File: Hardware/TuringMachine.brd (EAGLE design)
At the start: 107 x 49.5 mm, 83 parts, among them IC1 TL072P, IC2 4015, IC3 4015, IC5 4016, IC6 TL072P, IC7 TL072P, T1 2N3904, T2 2N3904, T3 2N3904

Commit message: Update R32 in noise and R6 in CV input
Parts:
- R32: value 10k -> 1k
- R6: value 150k -> 47k
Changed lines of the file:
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@@
 <grid distance="50" unitdist="mil" unit="mil" style="dots" multiple="1" display="no" altdistance="25" altunitdist="mil" altunit="mil"/>
 <layers>
-<layer number="1" name="Top" color="4" fill="1" visible="yes" active="yes"/>
+<layer number="1" name="Top" color="4" fill="1" visible="no" active="yes"/>
 <layer number="2" name="Route2" color="1" fill="3" visible="no" active="yes"/>
 <layer number="3" name="Route3" color="4" fill="3" visible="no" active="no"/>
 <layer number="14" name="Route14" color="1" fill="6" visible="no" active="no"/>
 <layer number="15" name="Route15" color="4" fill="6" visible="no" active="yes"/>
-<layer number="16" name="Bottom" color="1" fill="1" visible="yes" active="yes"/>
+<layer number="16" name="Bottom" color="1" fill="1" visible="no" active="yes"/>
 <layer number="17" name="Pads" color="10" fill="1" visible="yes" active="yes"/>
 <layer number="18" name="Vias" color="2" fill="1" visible="yes" active="yes"/>
@@
 <element name="R30" library="TomW" package="0207/7" value="10k" x="35.56" y="11.43"/>
 <element name="R31" library="TomW" package="0207/7" value="470k" x="45.72" y="12.7"/>
-<element name="R32" library="TomW" package="0207/7" value="10k" x="55.88" y="19.05"/>
+<element name="R32" library="TomW" package="0207/7" value="1k" x="55.88" y="19.05"/>
 <element name="NOISE-OUT" library="MusicThingModular" package="THONKICONN" value="THONKICONN" x="6.35" y="18.415" locked="yes" rot="R90"/>
 <element name="C2" library="TomW" package="C050-024X044" value="1n" x="17.145" y="38.1"/>
@@
 <element name="CV_IN" library="MusicThingModular" package="THONKICONN" value="THONKICONN" x="6.35" y="31.115" locked="yes" rot="R90"/>
 <element name="R5" library="TomW" package="0207/7" value="51k" x="5.715" y="24.765"/>
-<element name="R6" library="TomW" package="0207/7" value="150k" x="69.85" y="12.7"/>
+<element name="R6" library="TomW" package="0207/7" value="47k" x="69.85" y="12.7"/>
 <element name="CV_OUT" library="MusicThingModular" package="THONKICONN" value="THONKICONN" x="6.35" y="5.715" locked="yes" rot="R90"/>
 <element name="C13" library="TomW" package="C050-024X044" value="100n" x="66.04" y="33.02" rot="R90"/>

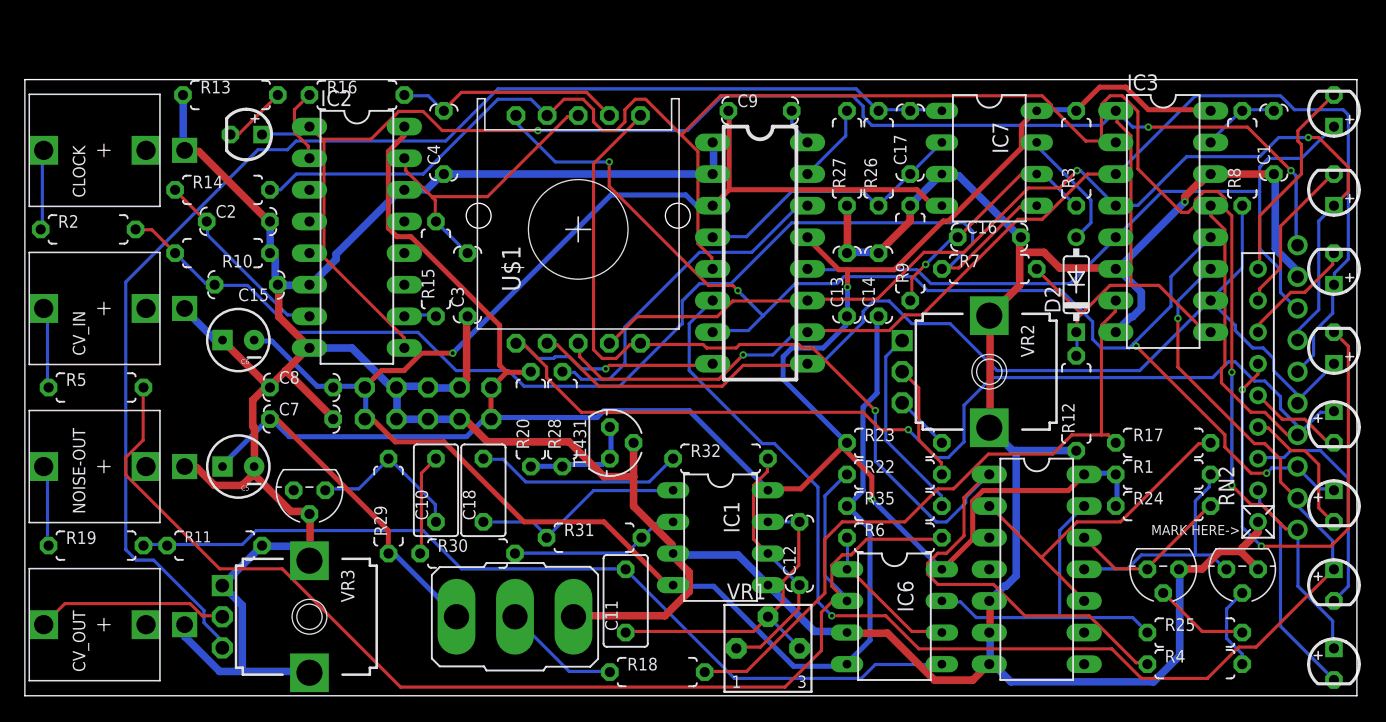
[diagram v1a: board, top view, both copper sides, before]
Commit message: Move R16 & C4 to start of loop
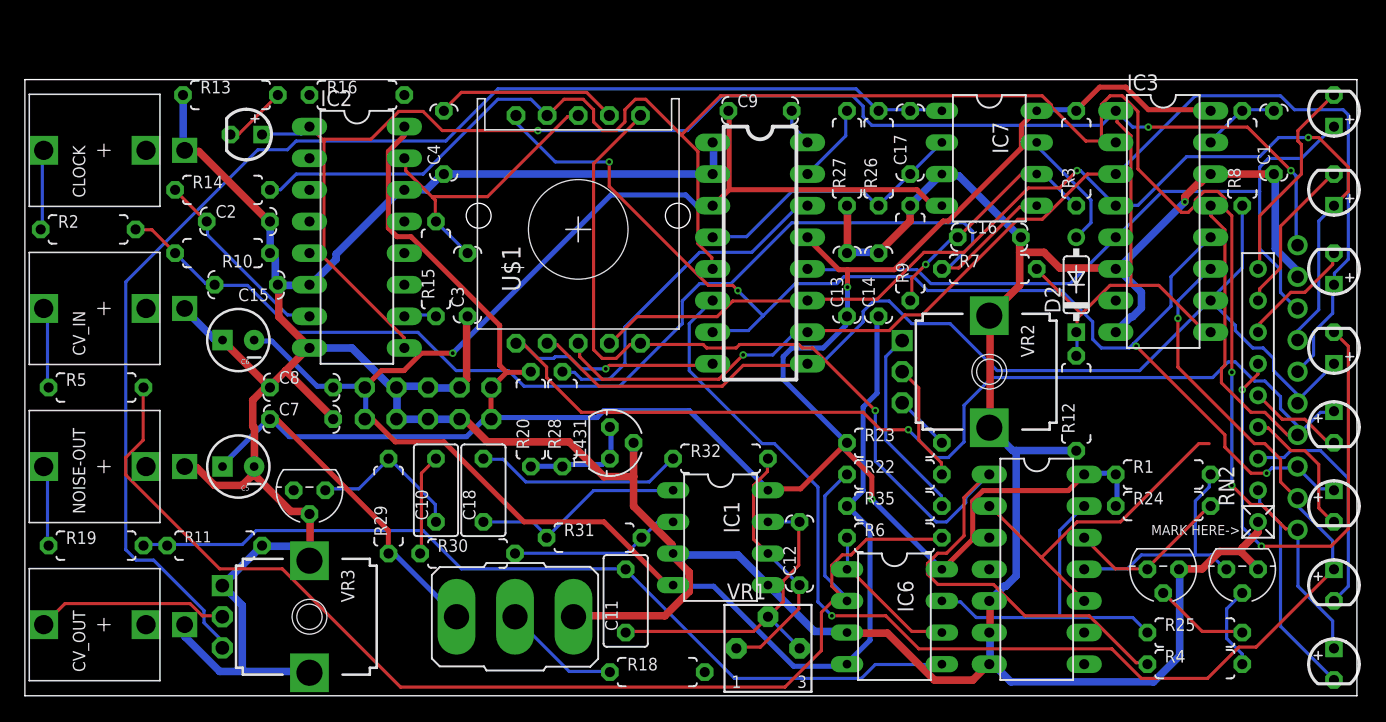
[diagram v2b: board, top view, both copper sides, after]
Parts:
- removed R17: 1k, TomW:0207/7
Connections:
- removed net N$19: IC3.7, R17.1, R18.2
- removed net N$29: IC2.2, R16.1
- net START_OF_LOOP: now also C4.2, IC3.7, R16.1, R16.2, R18.2; no longer R17.2
- net STEP_16: now also IC2.2; no longer C4.2, R16.2
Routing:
- net N$19: track 55.0 -> 0.00 mm
- net N$29: track 6.08 -> 0.00 mm
- net STEP_16: track 18.4 -> 14.6 mm
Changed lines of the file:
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@@
 <grid distance="50" unitdist="mil" unit="mil" style="dots" multiple="1" display="no" altdistance="25" altunitdist="mil" altunit="mil"/>
 <layers>
-<layer number="1" name="Top" color="4" fill="1" visible="no" active="yes"/>
+<layer number="1" name="Top" color="4" fill="1" visible="yes" active="yes"/>
 <layer number="2" name="Route2" color="1" fill="3" visible="no" active="yes"/>
 <layer number="3" name="Route3" color="4" fill="3" visible="no" active="no"/>
 <layer number="14" name="Route14" color="1" fill="6" visible="no" active="no"/>
 <layer number="15" name="Route15" color="4" fill="6" visible="no" active="yes"/>
-<layer number="16" name="Bottom" color="1" fill="1" visible="no" active="yes"/>
+<layer number="16" name="Bottom" color="1" fill="1" visible="yes" active="yes"/>
 <layer number="17" name="Pads" color="10" fill="1" visible="yes" active="yes"/>
 <layer number="18" name="Vias" color="2" fill="1" visible="yes" active="yes"/>
-<layer number="19" name="Unrouted" color="6" fill="1" visible="yes" active="yes"/>
+<layer number="19" name="Unrouted" color="6" fill="1" visible="no" active="yes"/>
 <layer number="20" name="Dimension" color="15" fill="1" visible="yes" active="yes"/>
 <layer number="21" name="tPlace" color="7" fill="1" visible="yes" active="yes"/>
-<layer number="22" name="bPlace" color="7" fill="1" visible="yes" active="yes"/>
-<layer number="23" name="tOrigins" color="15" fill="1" visible="yes" active="yes"/>
-<layer number="24" name="bOrigins" color="15" fill="1" visible="yes" active="yes"/>
+<layer number="22" name="bPlace" color="7" fill="1" visible="no" active="yes"/>
+<layer number="23" name="tOrigins" color="15" fill="1" visible="no" active="yes"/>
+<layer number="24" name="bOrigins" color="15" fill="1" visible="no" active="yes"/>
 <layer number="25" name="tNames" color="7" fill="1" visible="yes" active="yes"/>
 <layer number="26" name="bNames" color="7" fill="1" visible="no" active="yes"/>
-<layer number="27" name="tValues" color="7" fill="1" visible="no" active="yes"/>
+<layer number="27" name="tValues" color="7" fill="1" visible="yes" active="yes"/>
 <layer number="28" name="bValues" color="7" fill="1" visible="no" active="yes"/>
 <layer number="29" name="tStop" color="7" fill="3" visible="no" active="yes"/>
@@
 <layer number="49" name="Reference" color="7" fill="1" visible="no" active="yes"/>
 <layer number="50" name="dxf" color="7" fill="1" visible="no" active="no"/>
-<layer number="51" name="tDocu" color="7" fill="1" visible="yes" active="yes"/>
+<layer number="51" name="tDocu" color="7" fill="1" visible="no" active="yes"/>
 <layer number="52" name="bDocu" color="7" fill="1" visible="no" active="yes"/>
 <layer number="53" name="tGND_GNDA" color="7" fill="9" visible="no" active="no"/>
@@
 <element name="R9" library="TomW" package="0207/7" value="15k" x="71.12" y="35.56" rot="R90"/>
 <element name="WRITE" library="TomW" package="M9040P" value="T-80-T-SPDT-ON-OFF-ON" x="39.37" y="6.35" smashed="yes" rot="R90"/>
-<element name="R17" library="TomW" package="0207/7" value="1k" x="91.44" y="20.32"/>
 <element name="R18" library="TomW" package="0207/7" value="1k" x="50.8" y="1.905"/>
 <element name="EXPANSION" library="TomW" package="MA10-1" value="" x="102.235" y="24.765" locked="yes" rot="MR90">
@@
 </signal>
 <signal name="STEP_16">
-<contactref element="R16" pad="2"/>
-<contactref element="C4" pad="2"/>
 <contactref element="U$1" pad="H"/>
-<wire x1="32.4104" y1="48.1965" x2="30.5943" y2="48.1965" width="0.254" layer="16"/>
-<wire x1="33.528" y1="47.0789" x2="32.4104" y2="48.1965" width="0.254" layer="16"/>
-<wire x1="30.5943" y1="48.1965" x2="30.48" y2="48.26" width="0.254" layer="16"/>
-<wire x1="33.528" y1="47.0789" x2="33.655" y2="46.99" width="0.254" layer="16"/>
 <wire x1="45.1231" y1="48.4759" x2="46.9392" y2="46.6598" width="0.254" layer="1"/>
 <wire x1="35.0647" y1="48.4759" x2="45.1231" y2="48.4759" width="0.254" layer="1"/>
 <wire x1="33.6677" y1="47.0789" x2="35.0647" y2="48.4759" width="0.254" layer="1"/>
 <wire x1="46.9392" y1="46.6598" x2="46.95" y2="46.615" width="0.254" layer="1"/>
-<wire x1="33.6677" y1="47.0789" x2="33.655" y2="46.99" width="0.254" layer="1"/>
-</signal>
-<signal name="N$19">
-<contactref element="IC3" pad="7"/>
-<contactref element="R17" pad="1"/>
-<contactref element="R18" pad="2"/>
-<wire x1="57.9755" y1="1.9558" x2="54.6227" y2="1.9558" width="0.254" layer="1"/>
-<wire x1="64.262" y1="8.2423" x2="57.9755" y2="1.9558" width="0.254" layer="1"/>
-<wire x1="64.262" y1="12.573" x2="64.262" y2="8.2423" width="0.254" layer="1"/>
-<wire x1="65.659" y1="13.97" x2="64.262" y2="12.573" width="0.254" layer="1"/>
-<wire x1="70.6882" y1="13.97" x2="65.659" y2="13.97" width="0.254" layer="1"/>
-<wire x1="73.3425" y1="16.6243" x2="70.6882" y2="13.97" width="0.254" layer="1"/>
-<wire x1="74.5998" y1="16.6243" x2="73.3425" y2="16.6243" width="0.254" layer="1"/>
-<wire x1="77.3938" y1="19.4183" x2="74.5998" y2="16.6243" width="0.254" layer="1"/>
-<wire x1="82.5627" y1="19.4183" x2="77.3938" y2="19.4183" width="0.254" layer="1"/>
-<wire x1="84.0994" y1="20.955" x2="82.5627" y2="19.4183" width="0.254" layer="1"/>
-<wire x1="87.0331" y1="20.955" x2="86.4743" y2="20.955" width="0.254" layer="1"/>
-<wire x1="86.4743" y1="20.955" x2="84.0994" y2="20.955" width="0.254" layer="1"/>
-<wire x1="87.5919" y1="20.3962" x2="87.0331" y2="20.955" width="0.254" layer="1"/>
-<wire x1="54.6227" y1="1.9558" x2="54.61" y2="1.905" width="0.254" layer="1"/>
-<wire x1="87.5919" y1="20.3962" x2="87.63" y2="20.32" width="0.254" layer="1"/>
-<wire x1="87.5919" y1="30.8737" x2="87.5919" y2="31.7119" width="0.254" layer="1"/>
-<wire x1="86.4743" y1="29.7561" x2="87.5919" y2="30.8737" width="0.254" layer="1"/>
-<wire x1="86.4743" y1="20.955" x2="86.4743" y2="29.7561" width="0.254" layer="1"/>
-<wire x1="87.5919" y1="31.7119" x2="87.63" y2="31.75" width="0.254" layer="1"/>
+<contactref element="IC2" pad="2"/>
+<wire x1="22.86" y1="43.18" x2="33.6677" y2="47.0789" width="0" layer="19" extent="1-1"/>
 </signal>
 <signal name="B5">
@@
 </signal>
 <signal name="START_OF_LOOP">
-<contactref element="R17" pad="2"/>
 <contactref element="IC5" pad="10"/>
 <contactref element="IC5" pad="2"/>
@@
 <wire x1="84.5185" y1="13.97" x2="88.011" y2="13.97" width="0.254" layer="1"/>
 <wire x1="81.65465" y1="11.10615" x2="84.5185" y2="13.97" width="0.254" layer="1"/>
-<wire x1="95.1357" y1="20.2565" x2="95.25" y2="20.32" width="0.254" layer="1"/>
+<contactref element="R18" pad="2"/>
+<contactref element="IC3" pad="7"/>
+<contactref element="R16" pad="2"/>
+<contactref element="R16" pad="1"/>
+<contactref element="C4" pad="2"/>
+<wire x1="94.2975" y1="20.2565" x2="87.63" y2="31.75" width="0" layer="19" extent="1-1"/>
+<wire x1="54.61" y1="1.905" x2="77.47" y2="15.24" width="0" layer="19" extent="1-1"/>
+<wire x1="33.655" y1="46.99" x2="54.61" y2="1.905" width="0" layer="19" extent="1-1"/>
+<wire x1="30.48" y1="48.26" x2="33.655" y2="46.99" width="0" layer="19" extent="1-1"/>
+<wire x1="22.86" y1="48.26" x2="30.48" y2="48.26" width="0" layer="19" extent="1-1"/>
 </signal>
 <signal name="N$11">
@@
 <wire x1="105.0544" y1="1.397" x2="105.156" y2="1.27" width="0.254" layer="16"/>
 </signal>
-<signal name="N$29">
-<contactref element="R16" pad="1"/>
-<contactref element="IC2" pad="2"/>
-<wire x1="22.7711" y1="44.1452" x2="22.7711" y2="43.307" width="0.254" layer="1"/>
-<wire x1="21.6535" y1="45.2628" x2="22.7711" y2="44.1452" width="0.254" layer="1"/>
-<wire x1="21.6535" y1="47.0789" x2="21.6535" y2="45.2628" width="0.254" layer="1"/>
-<wire x1="22.7711" y1="48.1965" x2="21.6535" y2="47.0789" width="0.254" layer="1"/>
-<wire x1="22.7711" y1="43.307" x2="22.86" y2="43.18" width="0.254" layer="1"/>
-<wire x1="22.7711" y1="48.1965" x2="22.86" y2="48.26" width="0.254" layer="1"/>
-</signal>
 <signal name="N$39">

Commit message: Remove transistors, replace with 4016 gates
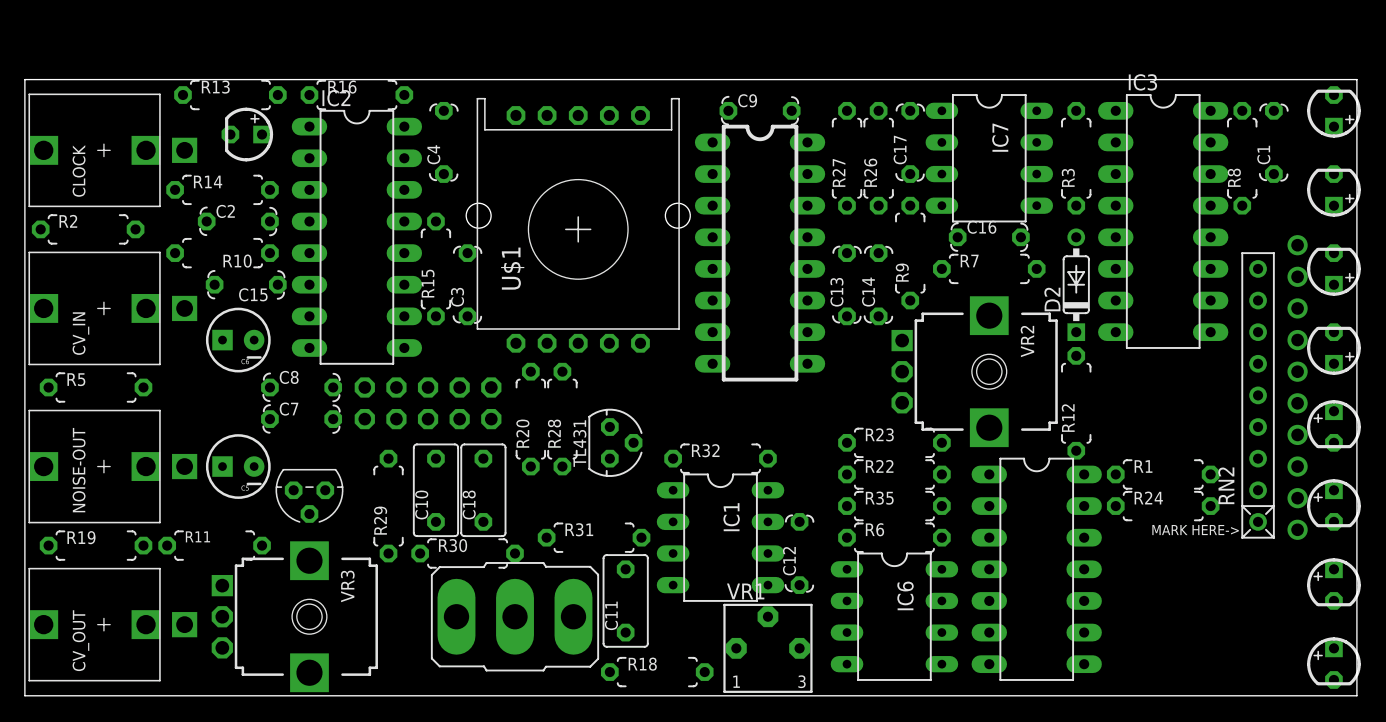
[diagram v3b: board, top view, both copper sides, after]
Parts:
- removed R25, R4: 100k, TomW:0207/7
- removed T2, T3: 2N3904, transistor:TO92
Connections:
- removed net N$1: R4.2, T3.2
- removed net N$44: R25.2, T2.2
- net END_OF_LOOP: now also IC5.5; no longer R4.1
- net GND: now also IC5.3, IC5.9; no longer IC5.5, IC5.6, T2.3, T3.3
- net N$24: now also IC5.6; no longer R25.1
- net N$4: now also IC5.4; no longer T3.1
- net N$45: now also IC5.8; no longer T2.1
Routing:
- net GND: track 376.9 -> 0.00 mm, vias 1 -> 0
- net +12V: track 207.7 -> 0.00 mm, vias 2 -> 0
- net B1: track 152.9 -> 0.00 mm, vias 2 -> 0
- net CLOCKIN: track 151.8 -> 0.00 mm, vias 3 -> 0
- net -12V: track 151.4 -> 0.00 mm, vias 1 -> 0
- net B4: track 119.0 -> 0.00 mm, vias 2 -> 0
- net B2: track 108.4 -> 0.00 mm, vias 2 -> 0
- net MAIN_OUT: track 106.4 -> 0.00 mm
- net N$6: track 101.8 -> 0.00 mm
- net B3: track 100.2 -> 0.00 mm, vias 4 -> 0
- net B6: track 96.1 -> 0.00 mm, vias 1 -> 0
- net END_OF_LOOP: track 94.7 -> 0.00 mm, vias 1 -> 0
- net N$5: track 93.3 -> 0.00 mm
- net B5: track 87.6 -> 0.00 mm
- net B7: track 85.2 -> 0.00 mm, vias 2 -> 0
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
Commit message: Fixes #5, fixes #4
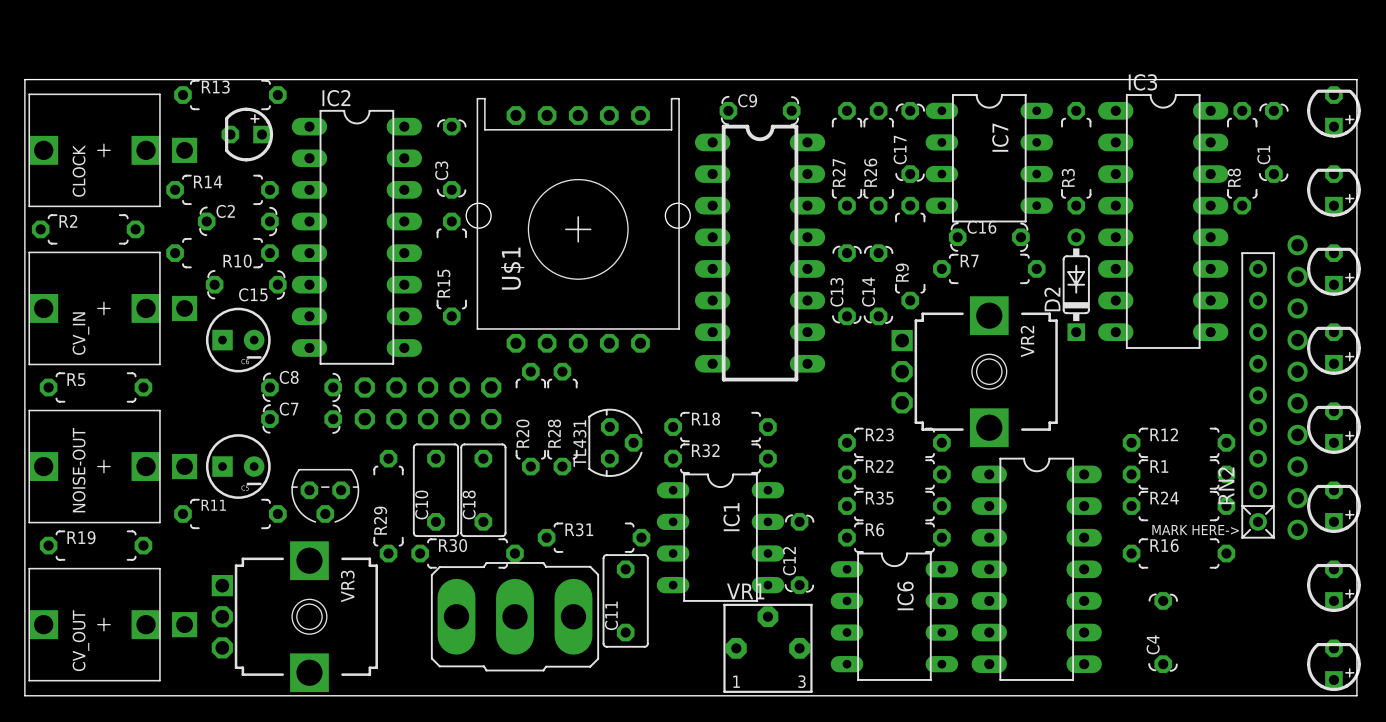
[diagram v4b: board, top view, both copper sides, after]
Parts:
- moved R16 75.6 mm to (92.7, 11.4)
- moved C4 69.9 mm to (91.4, 5.08)
- moved R18 20.3 mm to (55.9, 21.6)
- moved C3 10.2 mm to (34.3, 43.2)
- moved R12 8.84 mm to (92.7, 20.3), turned to 0 degrees
- moved R11 2.84 mm to (16.5, 14.6)
- moved T1 1.27 mm to (24.1, 16.5)
- moved R1 1.27 mm to (92.7, 17.8)
- moved R15 1.27 mm to (34.3, 34.3)
- moved R24 1.27 mm to (92.7, 15.2)
- turned 1 to 90 degrees
- turned 2 to 90 degrees
- turned 3 to 90 degrees
- turned 4 to 90 degrees

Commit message: not yet routed
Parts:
- moved IC5 10.2 mm to (91.4, 8.89)
- moved C4 10.2 mm to (101.6, 5.08)
- moved R16 8.13 mm to (99.1, 6.35), turned to 90 degrees
- moved IC6 7.73 mm to (77.5, 5.08)
- moved R22 7.73 mm to (77.5, 16.5)
- moved R23 7.73 mm to (77.5, 19.1)
- moved R35 7.73 mm to (77.5, 14.0)
- moved R6 7.73 mm to (77.5, 11.4)
- moved C12 6.35 mm to (68.6, 11.4)
- moved R24 5.24 mm to (91.4, 20.3)
- moved R1 5.24 mm to (91.4, 22.9)
- moved R12 5.24 mm to (91.4, 25.4)
- moved C9 5.08 mm to (59.1, 52.1)
- moved C5 4.58 mm to (14.6, 22.2)
- moved R18 4.02 mm to (59.7, 22.9)
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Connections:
- net +12V: now also R1.2, R24.2; no longer R1.1, R24.1
- net N$4: now also R1.1; no longer R1.2
- net N$45: now also R24.1; no longer R24.2
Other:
- board text added: "Music Thing Modular Turing Machine Rev 4 Prototype 2 July 2015 CC-BY-SA"
- board text removed: "Music Thing Modular Turing Machine Rev 4 Prototype 1 March 2015 CC-BY-SA"
